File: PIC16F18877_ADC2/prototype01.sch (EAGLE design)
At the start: 34 parts, among them CN1 12V_IN, CN2 ADC_IN, CN3 UART_IF, CN4 PIC_CN_H, CN5 AE-MICRO-SD-DIP, SW1 10-XX, U1 XC6202P332TH, U2 PIC16F18877-I/P, U3 AE-AQM1602A, U4 AE-RTC-8564NB

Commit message: 使用部品の見直し
回路じたいは変えていません。
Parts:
- C1, C2, C4, C5, C6, C7, C8: device Parts:CAP_200MIL -> Parts:CAP_100MIL
- C3: device Parts:ELECAP_200MIL -> Parts:ELECAP_D5_100MIL
- R1, R2, R3, R4, R5, R6, R7, R8, R9: device Parts:RESISTOR_300MIL -> Parts:RESISTOR_200MIL
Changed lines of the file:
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@@
 <parts>
 <part name="U2" library="Parts" deviceset="PIC16F18877*" device="-I/P"/>
-<part name="C4" library="Parts" deviceset="CAP" device="_200MIL" value="0.1uF"/>
-<part name="R1" library="Parts" deviceset="RESISTOR" device="_300MIL" value="10k"/>
+<part name="C4" library="Parts" deviceset="CAP" device="_100MIL" value="0.1uF"/>
+<part name="R1" library="Parts" deviceset="RESISTOR" device="_200MIL" value="10k"/>
 <part name="CN4" library="Connectors" deviceset="PIC_CN" device="_H"/>
 <part name="GND5" library="Supply" deviceset="0V" device=""/>
-<part name="C5" library="Parts" deviceset="CAP" device="_200MIL" value="0.1uF"/>
+<part name="C5" library="Parts" deviceset="CAP" device="_100MIL" value="0.1uF"/>
 <part name="SW1" library="Parts" deviceset="10-XX" device=""/>
 <part name="GND1" library="Supply" deviceset="0V" device=""/>
@@
 <part name="U3" library="PartsForProto" deviceset="AE-AQM1602A" device=""/>
 <part name="GND4" library="Supply" deviceset="0V" device=""/>
-<part name="R8" library="Parts" deviceset="RESISTOR" device="_300MIL" value="10k"/>
-<part name="R7" library="Parts" deviceset="RESISTOR" device="_300MIL" value="10k"/>
+<part name="R8" library="Parts" deviceset="RESISTOR" device="_200MIL" value="10k"/>
+<part name="R7" library="Parts" deviceset="RESISTOR" device="_200MIL" value="10k"/>
 <part name="GND3" library="Supply" deviceset="0V" device=""/>
 <part name="D1" library="Parts" deviceset="LED" device="_5MM"/>
-<part name="R2" library="Parts" deviceset="RESISTOR" device="_300MIL" value="330"/>
+<part name="R2" library="Parts" deviceset="RESISTOR" device="_200MIL" value="330"/>
 <part name="L1" library="Parts" deviceset="TC5026-22UH-060" device="" value="47uH"/>
 <part name="+3V3" library="Supply" deviceset="+3V3" device=""/>
 <part name="GND6" library="Supply" deviceset="0V" device=""/>
-<part name="C6" library="Parts" deviceset="CAP" device="_200MIL" value="10uF"/>
-<part name="R4" library="Parts" deviceset="RESISTOR" device="_300MIL" value="47k"/>
-<part name="R5" library="Parts" deviceset="RESISTOR" device="_300MIL" value="47k"/>
-<part name="R3" library="Parts" deviceset="RESISTOR" device="_300MIL" value="100k"/>
-<part name="R6" library="Parts" deviceset="RESISTOR" device="_300MIL" value="100k"/>
-<part name="C7" library="Parts" deviceset="CAP" device="_200MIL" value="0.1uF"/>
+<part name="C6" library="Parts" deviceset="CAP" device="_100MIL" value="10uF"/>
+<part name="R4" library="Parts" deviceset="RESISTOR" device="_200MIL" value="47k"/>
+<part name="R5" library="Parts" deviceset="RESISTOR" device="_200MIL" value="47k"/>
+<part name="R3" library="Parts" deviceset="RESISTOR" device="_200MIL" value="100k"/>
+<part name="R6" library="Parts" deviceset="RESISTOR" device="_200MIL" value="100k"/>
+<part name="C7" library="Parts" deviceset="CAP" device="_100MIL" value="0.1uF"/>
 <part name="CN3" library="PartsForProto" deviceset="UART_IF" device=""/>
 <part name="GND7" library="Supply" deviceset="0V" device=""/>
@@
 <part name="+3V2" library="Supply" deviceset="+3V3" device=""/>
 <part name="U1" library="Parts" deviceset="XC6202*" device="P332TH" value="XC6202P332TH"/>
-<part name="C1" library="Parts" deviceset="CAP" device="_200MIL" value="1uF"/>
-<part name="C2" library="Parts" deviceset="CAP" device="_200MIL" value="1uF"/>
+<part name="C1" library="Parts" deviceset="CAP" device="_100MIL" value="1uF"/>
+<part name="C2" library="Parts" deviceset="CAP" device="_100MIL" value="1uF"/>
 <part name="P+6" library="Supply" deviceset="+12V" device="" value="6V〜12V"/>
 <part name="GND8" library="Supply" deviceset="0V" device=""/>
@@
 <part name="+3V4" library="Supply" deviceset="+3V3" device=""/>
 <part name="U4" library="PartsForProto" deviceset="AE-RTC-8564NB" device=""/>
-<part name="C8" library="Parts" deviceset="CAP" device="_200MIL" value="0.1uF"/>
-<part name="R9" library="Parts" deviceset="RESISTOR" device="_300MIL" value="10k"/>
+<part name="C8" library="Parts" deviceset="CAP" device="_100MIL" value="0.1uF"/>
+<part name="R9" library="Parts" deviceset="RESISTOR" device="_200MIL" value="10k"/>
 <part name="GND14" library="Supply" deviceset="0V" device=""/>
 <part name="GND15" library="Supply" deviceset="0V" device=""/>
@@
 <part name="+3V8" library="Supply" deviceset="+3V" device=""/>
 <part name="G1" library="Parts" deviceset="CR2032H" device=""/>
-<part name="C3" library="Parts" deviceset="ELECAP" device="_200MIL" value="10uF"/>
+<part name="C3" library="Parts" deviceset="ELECAP" device="_D5_100MIL" value="10uF"/>
 <part name="FRAME1" library="Generic" deviceset="A3L-LOC" device=""/>
 <part name="GND9" library="Supply" deviceset="0V" device=""/>

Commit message: 使用部品の見直し
回路じたいは変えていません。
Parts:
- L1: device Parts:TC5026-22UH-060 -> Parts:LEAD_INDUCTOR
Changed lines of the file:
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@@
 <part name="D1" library="Parts" deviceset="LED" device="_5MM"/>
 <part name="R2" library="Parts" deviceset="RESISTOR" device="_200MIL" value="330"/>
-<part name="L1" library="Parts" deviceset="TC5026-22UH-060" device="" value="47uH"/>
+<part name="L1" library="Parts" deviceset="LEAD_INDUCTOR" device="" value="47uH"/>
 <part name="+3V3" library="Supply" deviceset="+3V3" device=""/>
 <part name="GND6" library="Supply" deviceset="0V" device=""/>

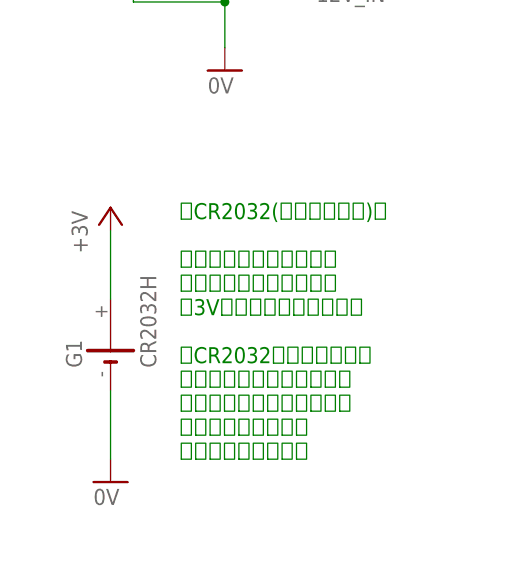
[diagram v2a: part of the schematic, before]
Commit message: 使用部品の見直し
電池ホルダー部品を差し替え
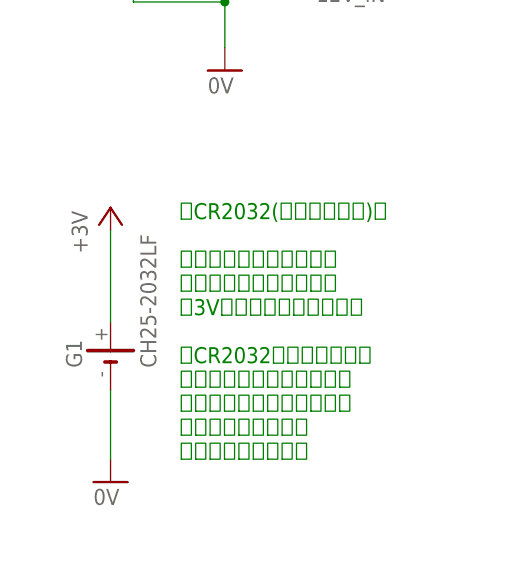
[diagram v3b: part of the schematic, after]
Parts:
- G1: value CR2032H -> CH25-2032LF; device Parts:CR2032H -> Parts:CH25-2032LF
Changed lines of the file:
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@@
 <part name="+3V7" library="Supply" deviceset="+3V" device=""/>
 <part name="+3V8" library="Supply" deviceset="+3V" device=""/>
-<part name="G1" library="Parts" deviceset="CR2032H" device=""/>
 <part name="C3" library="Parts" deviceset="ELECAP" device="_D5_100MIL" value="10uF"/>
 <part name="FRAME1" library="Generic" deviceset="A3L-LOC" device=""/>
 <part name="GND9" library="Supply" deviceset="0V" device=""/>
+<part name="G1" library="Parts" deviceset="CH25-2032LF" device=""/>
 </parts>
 <sheets>
@@
 <instance part="+3V7" gate="G$1" x="327.66" y="93.98"/>
 <instance part="+3V8" gate="G$1" x="50.8" y="124.46"/>
-<instance part="G1" gate="1" x="50.8" y="109.22" rot="R90"/>
 <instance part="C3" gate="G$1" x="53.34" y="157.48"/>
 <instance part="FRAME1" gate="G$1" x="0" y="0"/>
 <instance part="GND9" gate="1" x="327.66" y="58.42"/>
+<instance part="G1" gate="G$1" x="50.8" y="109.22" rot="R90"/>
 </instances>
 <busses>
@@
 </segment>
 <segment>
-<pinref part="GND15" gate="1" pin="0V"/>
-<pinref part="G1" gate="1" pin="-"/>
-<wire x1="50.8" y1="96.52" x2="50.8" y2="104.14" width="0.1524" layer="91"/>
-</segment>
-<segment>
 <pinref part="C8" gate="G$1" pin="2"/>
 <pinref part="GND9" gate="1" pin="0V"/>
 <wire x1="327.66" y1="66.04" x2="327.66" y2="60.96" width="0.1524" layer="91"/>
+</segment>
+<segment>
+<pinref part="GND15" gate="1" pin="0V"/>
+<pinref part="G1" gate="G$1" pin="-"/>
+<wire x1="50.8" y1="96.52" x2="50.8" y2="104.14" width="0.1524" layer="91"/>
 </segment>
 </net>
@@
 </segment>
 <segment>
-<pinref part="G1" gate="1" pin="+"/>
 <pinref part="+3V8" gate="G$1" pin="+3V"/>
-<wire x1="50.8" y1="114.3" x2="50.8" y2="121.92" width="0.1524" layer="91"/>
-</segment>
-</net>
+<pinref part="G1" gate="G$1" pin="+"/>
+<wire x1="50.8" y1="121.92" x2="50.8" y2="111.76" width="0.1524" layer="91"/>
+</segment>
+</net>

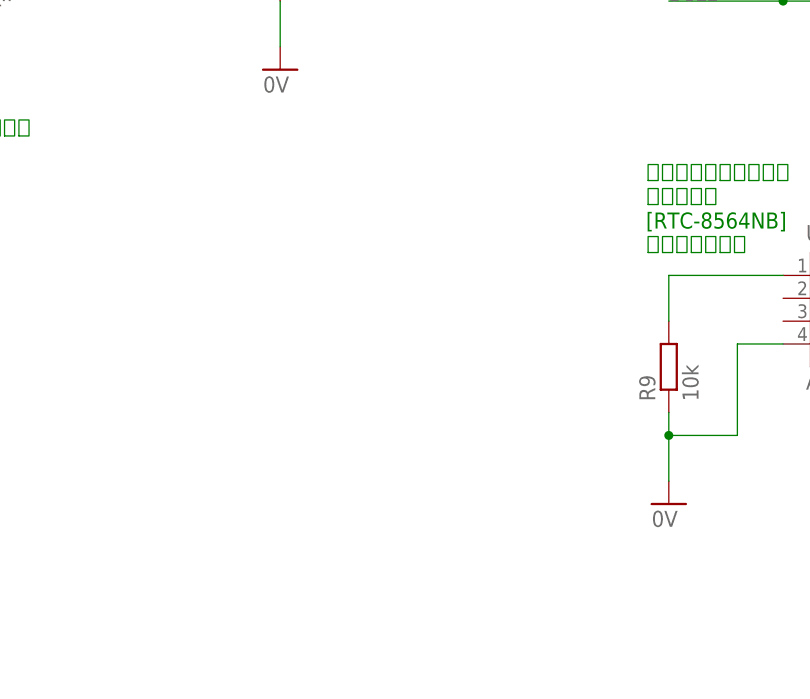
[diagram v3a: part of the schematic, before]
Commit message: 使用部品の見直し
microSD変換基板用コネクターのデザインを差し替え
I2Cインターフェース用品を追加
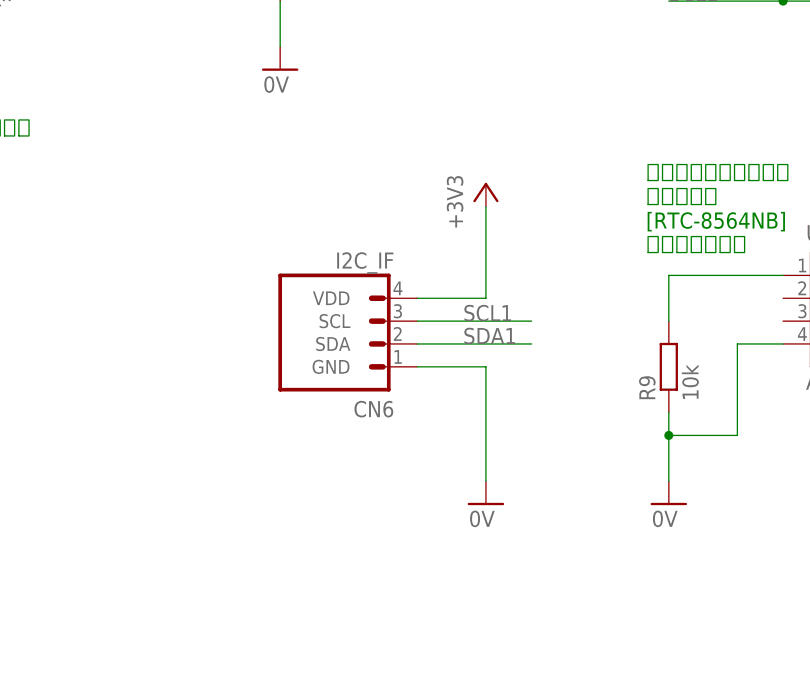
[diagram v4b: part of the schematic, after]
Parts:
- added CN6: I2C_IF, PartsForProto:I2C_IF
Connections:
- net +3V3: now also CN6.VDD
- net 0V: now also CN6.GND
- net SCL1: now also CN6.SCL
- net SDA1: now also CN6.SDA
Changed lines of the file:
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@@
 <part name="GND9" library="Supply" deviceset="0V" device=""/>
 <part name="G1" library="Parts" deviceset="CH25-2032LF" device=""/>
+<part name="CN6" library="PartsForProto" deviceset="I2C_IF" device=""/>
+<part name="+3V5" library="Supply" deviceset="+3V3" device=""/>
+<part name="GND11" library="Supply" deviceset="0V" device=""/>
 </parts>
 <sheets>
@@
 <instance part="GND9" gate="1" x="327.66" y="58.42"/>
 <instance part="G1" gate="G$1" x="50.8" y="109.22" rot="R90"/>
+<instance part="CN6" gate="G$1" x="246.38" y="73.66" rot="R180"/>
+<instance part="+3V5" gate="G$1" x="254" y="93.98"/>
+<instance part="GND11" gate="1" x="254" y="58.42"/>
 </instances>
 <busses>
@@
 <wire x1="50.8" y1="96.52" x2="50.8" y2="104.14" width="0.1524" layer="91"/>
 </segment>
+<segment>
+<pinref part="CN6" gate="G$1" pin="GND"/>
+<pinref part="GND11" gate="1" pin="0V"/>
+<wire x1="246.38" y1="73.66" x2="254" y2="73.66" width="0.1524" layer="91"/>
+<wire x1="254" y1="73.66" x2="254" y2="60.96" width="0.1524" layer="91"/>
+</segment>
 </net>
 <net name="N$3" class="0">
@@
 <label x="317.5" y="78.74" size="1.778" layer="95"/>
 </segment>
+<segment>
+<pinref part="CN6" gate="G$1" pin="SCL"/>
+<wire x1="246.38" y1="78.74" x2="259.08" y2="78.74" width="0.1524" layer="91"/>
+<label x="251.46" y="78.74" size="1.778" layer="95"/>
+</segment>
 </net>
 <net name="SDA1" class="0">
@@
 <wire x1="314.96" y1="76.2" x2="325.12" y2="76.2" width="0.1524" layer="91"/>
 <label x="317.5" y="76.2" size="1.778" layer="95"/>
+</segment>
+<segment>
+<pinref part="CN6" gate="G$1" pin="SDA"/>
+<wire x1="246.38" y1="76.2" x2="259.08" y2="76.2" width="0.1524" layer="91"/>
+<label x="251.46" y="76.2" size="1.778" layer="95"/>
 </segment>
 </net>
@@
 <junction x="45.72" y="210.82"/>
 </segment>
-</net>
+<segment>
+<pinref part="CN6" gate="G$1" pin="VDD"/>
+<wire x1="246.38" y1="81.28" x2="254" y2="81.28" width="0.1524" layer="91"/>
+<pinref part="+3V5" gate="G$1" pin="+3V3"/>
+<wire x1="254" y1="81.28" x2="254" y2="91.44" width="0.1524" layer="91"/>
+</segment>
+</net>
